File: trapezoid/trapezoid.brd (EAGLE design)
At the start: 59.7 x 28.6 mm, 33 parts, among them U1 MMA8452Q, U2 microSD, U4 MCP73831, Y1 CRYSTAL.ABS25

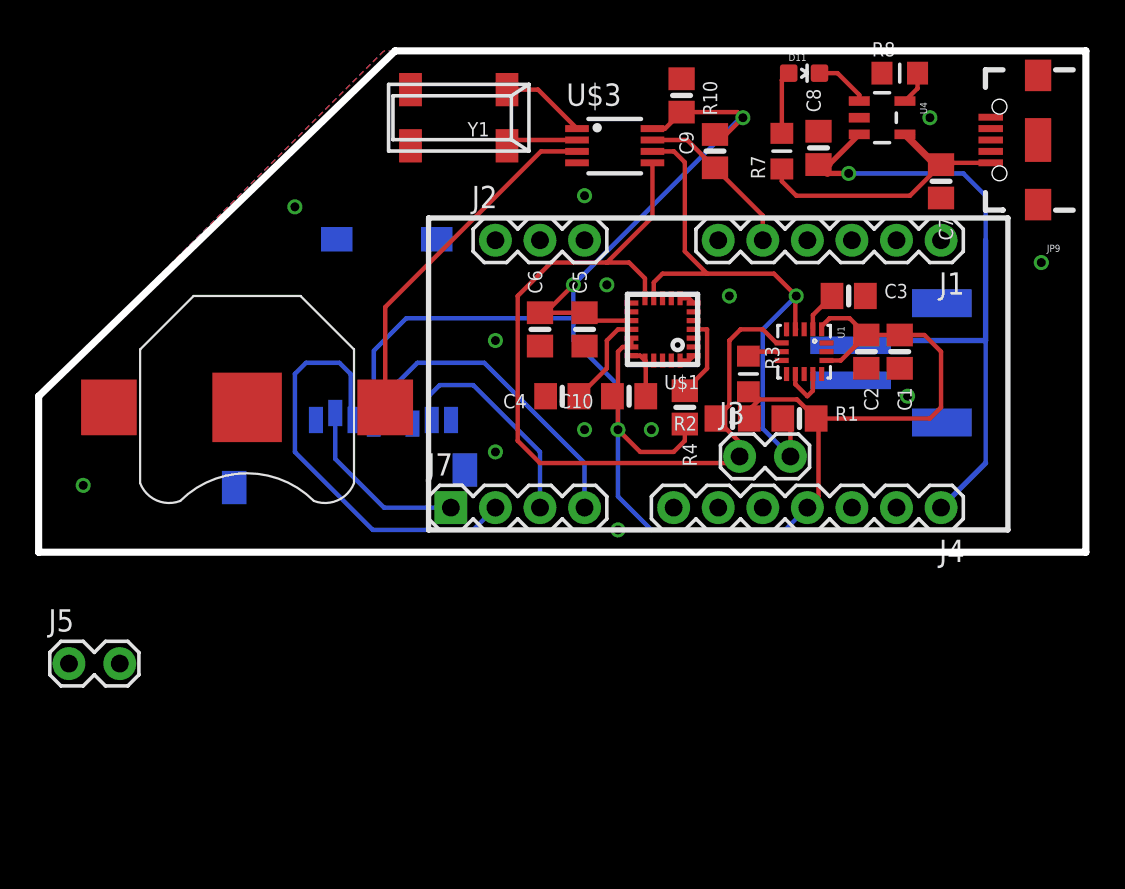
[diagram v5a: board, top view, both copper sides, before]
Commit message: put new uSD slot on board
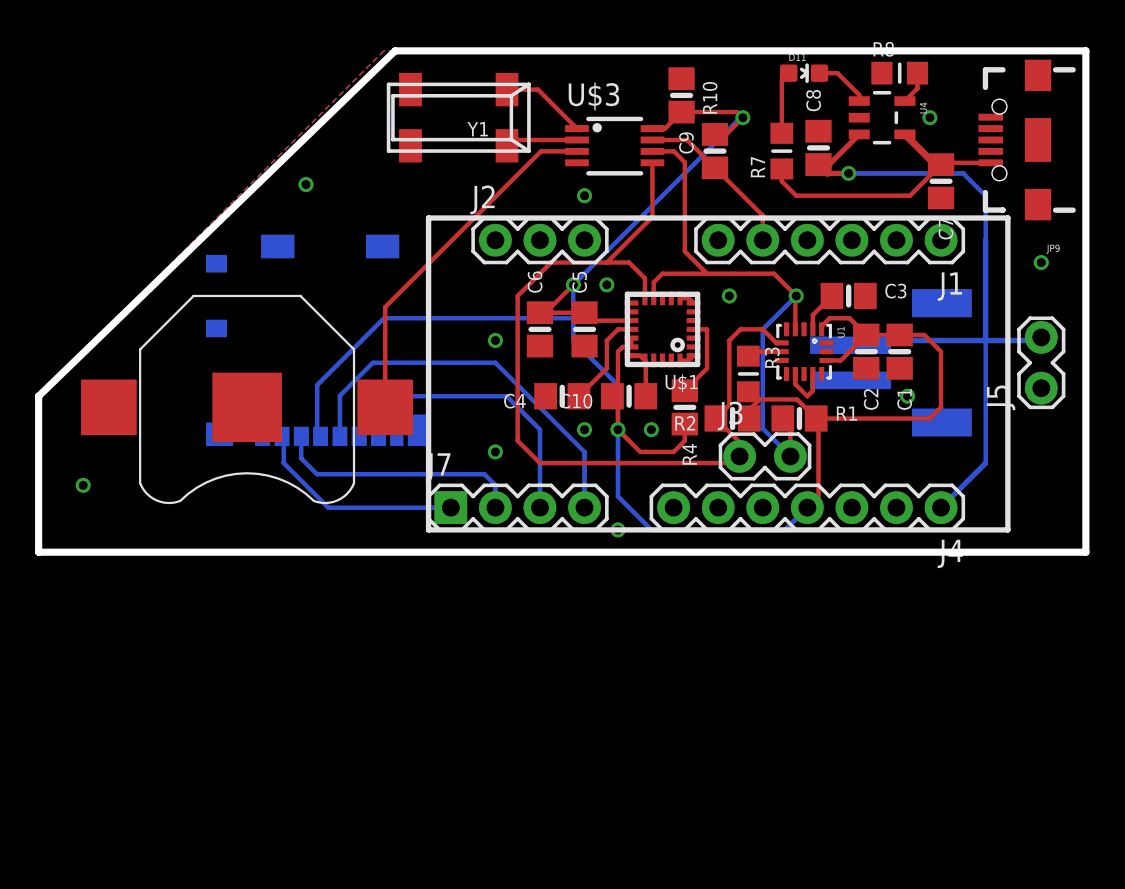
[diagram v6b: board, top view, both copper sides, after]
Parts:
- removed U2: microSD, SparkFun:MICRO-SD-SOCKET-PP
- added U$2: MOLEX_MICROSD, sharkdunio:MOLEX_MICROSD
- moved J5 57.5 mm to (57.1, 9.53), turned to 90 degrees
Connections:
- net +3V3: now also U$2.4; no longer U2.4
- net GND: now also U$2.11, U$2.12, U$2.13, U$2.14, U$2.6; no longer U2.6, U2.GND1, U2.GND2
- net MISO: now also U$2.7; no longer U2.7
- net MOSI: now also U$2.3; no longer U2.3
- net SCK: now also U$2.5; no longer U2.5
- net SD_CS: now also U$2.2; no longer U2.2
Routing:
- net MOSI: track 24.7 -> 14.2 mm
- net SCK: track 18.3 -> 22.3 mm
- net MISO: track 12.8 -> 16.2 mm
- net V_RAW: track 39.9 -> 43.2 mm
- net +3V3: track 115.4 -> 118.3 mm
- net SD_CS: track 10.4 -> 12.1 mm
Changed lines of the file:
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@@
 <setting verticaltext="up"/>
 </settings>
-<grid distance="0.025" unitdist="inch" unit="inch" style="lines" multiple="1" display="yes" altdistance="0.025" altunitdist="inch" altunit="inch"/>
+<grid distance="0.025" unitdist="inch" unit="inch" style="lines" multiple="1" display="yes" altdistance="0.005" altunitdist="inch" altunit="inch"/>
 <layers>
 <layer number="1" name="Top" color="4" fill="1" visible="yes" active="yes"/>
@@
 <element name="R8" library="microbuilder" package="_0805MP" value="2.0k" x="49.08" y="27.305"/>
 <element name="U1" library="SparkFun" package="QFN-16_0.5MM" value="MMA8452Q" x="43.63" y="11.43" rot="R270"/>
-<element name="U2" library="SparkFun" package="MICRO-SD-SOCKET-PP" value="microSD" x="24.745" y="18.235" rot="MR180"/>
 <element name="U4" library="SparkFun-PowerIC" package="SOT23-5" value="MCP73831" x="48.075" y="24.765" rot="R270">
 <attribute name="PROD_ID" value="IC-09995" x="48.075" y="24.765" size="1.778" layer="27" rot="R270" display="off"/>
@@
 <element name="C5" library="microbuilder" package="0805-NO" value="0.1uF" x="31.115" y="12.7" rot="R90"/>
 <element name="C6" library="microbuilder" package="0805-NO" value="0.1uF" x="28.575" y="12.7" rot="R90"/>
-<element name="J5" library="SparkFun-Connectors" package="1X02_LOCK" value="" x="1.905" y="-6.35"/>
+<element name="J5" library="SparkFun-Connectors" package="1X02_LOCK" value="" x="57.15" y="9.525" rot="R90"/>
+<element name="U$2" library="sharkdunio" package="MOLEX_MICROSD" value="MOLEX_MICROSD" x="15.875" y="6.35" rot="MR0"/>
 </elements>
 <signals>
@@
 <contactref element="C1" pad="2"/>
 <contactref element="C2" pad="2"/>
-<contactref element="U2" pad="6"/>
-<contactref element="U2" pad="GND1"/>
-<contactref element="U2" pad="GND2"/>
 <contactref element="C8" pad="2"/>
 <contactref element="C7" pad="2"/>
@@
 <via x="39.37" y="14.605" extent="1-16" drill="0.508"/>
 <via x="31.115" y="20.32" extent="1-16" drill="0.508"/>
-<via x="14.605" y="19.685" extent="1-16" drill="0.508"/>
+<via x="15.24" y="20.955" extent="1-16" drill="0.508"/>
 <via x="26.035" y="5.715" extent="1-16" drill="0.508"/>
 <via x="57.15" y="16.51" extent="1-16" drill="0.508"/>
@@
 <via x="26.035" y="12.065" extent="1-16" drill="0.508"/>
 <contactref element="J5" pad="1"/>
-<wire x1="2.54" y1="3.81" x2="1.7272" y2="-6.35" width="0" layer="19" extent="1-1"/>
+<contactref element="U$2" pad="6"/>
+<contactref element="U$2" pad="14"/>
+<contactref element="U$2" pad="13"/>
+<contactref element="U$2" pad="12"/>
+<contactref element="U$2" pad="11"/>
 </signal>
 <signal name="SCL">
@@
 </signal>
 <signal name="SD_CS">
-<contactref element="U2" pad="2"/>
 <contactref element="J7" pad="1"/>
-<wire x1="16.905" y1="7.935" x2="16.905" y2="5.32" width="0.254" layer="16"/>
-<wire x1="16.905" y1="5.32" x2="19.685" y2="2.54" width="0.254" layer="16"/>
-<wire x1="19.685" y1="2.54" x2="23.495" y2="2.54" width="0.254" layer="16"/>
+<wire x1="16.51" y1="2.54" x2="23.495" y2="2.54" width="0.254" layer="16"/>
+<contactref element="U$2" pad="2"/>
+<wire x1="16.51" y1="2.54" x2="13.97" y2="5.08" width="0.254" layer="16"/>
+<wire x1="13.97" y1="5.08" x2="13.97" y2="6.5" width="0.254" layer="16"/>
+<wire x1="13.97" y1="6.5" x2="13.87" y2="6.6" width="0.254" layer="16"/>
 </signal>
 <signal name="MOSI">
-<contactref element="U2" pad="3"/>
 <contactref element="J7" pad="2"/>
-<wire x1="14.605" y1="5.715" x2="14.605" y2="10.16" width="0.254" layer="16"/>
-<wire x1="14.605" y1="10.16" x2="15.24" y2="10.795" width="0.254" layer="16"/>
-<wire x1="15.24" y1="10.795" x2="17.145" y2="10.795" width="0.254" layer="16"/>
-<wire x1="17.145" y1="10.795" x2="17.78" y2="10.16" width="0.254" layer="16"/>
-<wire x1="17.78" y1="10.16" x2="17.78" y2="7.76" width="0.254" layer="16"/>
-<wire x1="17.78" y1="7.76" x2="18.005" y2="7.535" width="0.254" layer="16"/>
-<wire x1="14.605" y1="5.715" x2="19.05" y2="1.27" width="0.254" layer="16"/>
-<wire x1="19.05" y1="1.27" x2="24.765" y2="1.27" width="0.254" layer="16"/>
-<wire x1="24.765" y1="1.27" x2="26.035" y2="2.54" width="0.254" layer="16"/>
+<contactref element="U$2" pad="3"/>
+<wire x1="26.035" y1="2.54" x2="26.035" y2="3.81" width="0.254" layer="16"/>
+<wire x1="14.97" y1="6.6" x2="14.97" y2="5.35" width="0.254" layer="16"/>
+<wire x1="14.97" y1="5.35" x2="15.875" y2="4.445" width="0.254" layer="16"/>
+<wire x1="15.875" y1="4.445" x2="25.4" y2="4.445" width="0.254" layer="16"/>
+<wire x1="25.4" y1="4.445" x2="26.035" y2="3.81" width="0.254" layer="16"/>
 </signal>
 <signal name="SCK">
-<contactref element="U2" pad="5"/>
 <contactref element="J7" pad="4"/>
-<wire x1="20.205" y1="7.535" x2="20.205" y2="9.41" width="0.254" layer="16"/>
-<wire x1="20.205" y1="9.41" x2="21.59" y2="10.795" width="0.254" layer="16"/>
-<wire x1="31.115" y1="2.54" x2="31.115" y2="5.08" width="0.254" layer="16"/>
-<wire x1="31.115" y1="5.08" x2="25.4" y2="10.795" width="0.254" layer="16"/>
-<wire x1="25.4" y1="10.795" x2="21.59" y2="10.795" width="0.254" layer="16"/>
+<contactref element="U$2" pad="5"/>
+<wire x1="26.035" y1="10.795" x2="19.05" y2="10.795" width="0.254" layer="16"/>
+<wire x1="31.115" y1="2.54" x2="31.115" y2="5.715" width="0.254" layer="16"/>
+<wire x1="31.115" y1="5.715" x2="26.035" y2="10.795" width="0.254" layer="16"/>
+<wire x1="17.17" y1="8.915" x2="19.05" y2="10.795" width="0.254" layer="16"/>
+<wire x1="17.17" y1="6.6" x2="17.17" y2="8.915" width="0.254" layer="16"/>
 </signal>
 <signal name="MISO">
-<contactref element="U2" pad="7"/>
 <contactref element="J7" pad="3"/>
-<wire x1="22.86" y1="9.525" x2="24.765" y2="9.525" width="0.254" layer="16"/>
-<wire x1="24.765" y1="9.525" x2="28.575" y2="5.715" width="0.254" layer="16"/>
-<wire x1="28.575" y1="2.54" x2="28.575" y2="5.715" width="0.254" layer="16"/>
-<wire x1="22.86" y1="9.525" x2="22.225" y2="8.89" width="0.254" layer="16"/>
-<wire x1="22.225" y1="8.89" x2="22.225" y2="7.715" width="0.254" layer="16"/>
-<wire x1="22.225" y1="7.715" x2="22.405" y2="7.535" width="0.254" layer="16"/>
+<contactref element="U$2" pad="7"/>
+<wire x1="28.575" y1="6.985" x2="28.575" y2="2.54" width="0.254" layer="16"/>
+<wire x1="19.37" y1="6.6" x2="19.37" y2="7.94" width="0.254" layer="16"/>
+<wire x1="19.37" y1="7.94" x2="20.32" y2="8.89" width="0.254" layer="16"/>
+<wire x1="20.32" y1="8.89" x2="26.67" y2="8.89" width="0.254" layer="16"/>
+<wire x1="26.67" y1="8.89" x2="28.575" y2="6.985" width="0.254" layer="16"/>
 </signal>
 <signal name="V_RAW">
@@
 <wire x1="53.975" y1="20.32" x2="52.705" y2="21.59" width="0.254" layer="16"/>
 <contactref element="J5" pad="2"/>
-<wire x1="4.6228" y1="-6.35" x2="46.28" y2="11.795" width="0" layer="19" extent="16-16"/>
+<wire x1="53.975" y1="12.065" x2="56.9722" y2="12.065" width="0.3048" layer="16"/>
+<wire x1="56.9722" y1="12.065" x2="57.15" y2="12.2428" width="0.254" layer="16"/>
 </signal>
 <signal name="+3V3">
@@
 <contactref element="C2" pad="1"/>
 <contactref element="R3" pad="2"/>
-<contactref element="U2" pad="4"/>
 <contactref element="U$3" pad="8"/>
 <contactref element="C9" pad="2"/>
@@
 <via x="33.02" y="6.985" extent="1-16" drill="0.508"/>
 <wire x1="33.785" y1="11.7" x2="33.29" y2="11.7" width="0.254" layer="1"/>
-<wire x1="19.105" y1="7.335" x2="19.105" y2="11.485" width="0.254" layer="16"/>
 <wire x1="30.93" y1="13.2" x2="31.115" y2="13.65" width="0.254" layer="1"/>
 <wire x1="28.575" y1="13.65" x2="31.115" y2="13.65" width="0.254" layer="1"/>
@@
 <wire x1="33.02" y1="6.985" x2="33.02" y2="9.525" width="0.254" layer="16"/>
 <wire x1="33.02" y1="9.525" x2="30.48" y2="12.065" width="0.254" layer="16"/>
-<wire x1="19.105" y1="11.485" x2="20.955" y2="13.335" width="0.254" layer="16"/>
-<wire x1="20.955" y1="13.335" x2="30.48" y2="13.335" width="0.254" layer="16"/>
+<wire x1="19.685" y1="13.335" x2="30.48" y2="13.335" width="0.254" layer="16"/>
 <wire x1="34.925" y1="1.27" x2="33.02" y2="3.175" width="0.254" layer="16"/>
 <wire x1="33.02" y1="3.175" x2="33.02" y2="6.985" width="0.254" layer="16"/>
@@
 <wire x1="39.82" y1="25.085" x2="40.14" y2="24.765" width="0.254" layer="1"/>
 <wire x1="39.185" y1="23.81" x2="40.14" y2="24.765" width="0.254" layer="1"/>
+<contactref element="U$2" pad="4"/>
+<wire x1="19.685" y1="13.335" x2="15.875" y2="9.525" width="0.254" layer="16"/>
+<wire x1="15.875" y1="9.525" x2="15.875" y2="6.795" width="0.254" layer="16"/>
+<wire x1="15.875" y1="6.795" x2="16.07" y2="6.6" width="0.254" layer="16"/>
 </signal>
 <signal name="N$1">
